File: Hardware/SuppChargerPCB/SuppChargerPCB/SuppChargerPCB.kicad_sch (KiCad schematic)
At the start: 36 parts, among them J1 SLIMSTACK, J2 SLIMSTACK, Q1 NMOS, Q2 NMOS, Q3 NMOS, Q4 NMOS, U1 BQ25756ERRVR

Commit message: reorg
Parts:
- removed RT1: 103AT-2, 103AT2, symbol NTC10k:103AT-2
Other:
- moved on the sheet: C1, C11, C5, C6, C7, D4, D5, J1, J2, L1, Q1, Q2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

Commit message: need to add connector symbols, desmos
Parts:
- removed C10, C3: 0.1uF, symbol Device:C
- removed C11: 100nF, symbol Device:C
- removed C4: 1uF, symbol Device:C
- removed C6, C7: 80uF, symbol Device:C
- removed C8: 0.47uF, symbol Device:C
- removed D4, D5: D, symbol Device:D
- removed L1: 10uH, symbol Device:L
- removed Q1, Q2, Q3, Q4: NMOS, symbol Simulation_SPICE:NMOS
- added C11, C20, C21, C22, C6, C7: 56uF, symbol Device:C_Polarized_US
- added C16, C17, C18, C19, C23, C25: 100nF, symbol Device:C
- added C24: 470nF, symbol Device:C
- added D10, D9: Schottky, symbol Device:D_Schottky
- added D6, D7: LED, symbol Device:LED
- added H1, H2, H3: MountingHole, symbol Mechanical:MountingHole
- added L3: 2.2uH, symbol Device:L
- added Q10, Q7, Q8, Q9: NMOS, symbol NMOS_Buck:SI3456DDV-T1-GE3
- added R12, R13: 0, symbol Device:R
- added R14: 2m, symbol Device:R
- added R15, R16, R18, R19: 10, symbol Device:R
- added R17: 5m, symbol Device:R
- added R20: 249k, symbol Device:R
- added R21: 14.11K, symbol Device:R
- added R22: 133k, symbol Device:R
- C1: value 100nF -> 470nF
- C2: value 0.47uF -> 1uF
- C5: value 100uF -> 4.7uF
- C9: value 0.1uF -> 100nF
- R1: value 5.24k -> 1000k
- R10: value 30.31k -> 10k
- R11: value R -> 10k
- R2: value 10k -> 16k
- R3: value 10k -> 42k
- R4: value 249k -> 0
- R5: value 0.05 -> 0
- R6: value 133k -> 0
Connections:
- net BAT is gone; now on net OUT: J2.1, J2.2, J2.3, J2.4, J2.5, J2.6, J2.7, J2.8
- net VAC is gone; now on an unnamed net: R2.1
- net *CE: now also J2.19, D6.1 (K)
- net *INT: now also J2.13, D7.1 (K)
- net +24V: now also C2.1, R1.1, U1.32 (VAC), U1.33 (VAC), C6.1, C7.1, R14.1, R15.1; no longer J1.24
- net BTST1: now also C16.2, D9.1 (K)
- net BTST2: now also C17.2, D10.1 (K)
- net DRV_SUP: now also R4.1
- net FB: now also R20.2, R21.1; no longer R11.1, R4.2
- net FBG: now also R21.2; no longer R11.2
- net HIDRV1: now also R5.1
- net LODRV1: now also R6.1, R12.2
- net LODRV2: now also R13.2
- net PGND: now also U1.8 (TS), C11.2, C18.2, C19.2, C20.2, C21.2, C22.2, C23.2, C25.2, C6.2, C7.2, Q10.1 (S), Q10.2 (S), Q10.3 (S), Q8.1 (S), Q8.2 (S), Q8.3 (S), R22.1; no longer J2.17, J2.19, R10.2, R6.2
- net REGN: no longer R1.1, R7.1, R8.1, R9.1
- net SCL: now also J2.11
- net SDA: now also J2.9
- net STAT1: now also J2.15
- net STAT2: now also J2.17
- net SW1: now also C16.1, L3.1, Q7.1 (S), Q7.2 (S), Q7.3 (S), Q8.5 (D), Q8.6 (S), Q8.7 (S), Q8.8 (S); no longer C1.1
- net SW2: now also C17.1, L3.2, Q10.5 (D), Q10.6 (S), Q10.7 (S), Q10.8 (S), Q9.1 (S), Q9.2 (S), Q9.3 (S)
- net at C9.1: now also C2.2; no longer U1.13 (SRN)
- net at R5.2: now also Q7.4 (G)
- net ACP: now reaches C1.2
- net ACP: now also U1.30 (ACP), C18.1, R15.2
- net FSW: now reaches U1.36 (FSW_SYNC)
- net FSW: now also R22.2; no longer R6.1
- net ACN: now reaches U1.29 (ACN)
- net ACN: now also C1.1, C19.1, R16.2
- net SRP: now reaches U1.14 (SRP)
- net SRP: now also C23.1, C24.2, R18.2
- net OUT: now reaches J2.10
- net OUT: now also J2.12, J2.14, J2.16, C21.1, C22.1, R17.2, R19.1, R20.1
- net at U1.34 (ACUV): now also R1.2; no longer R2.2
- net at R3.1, U1.35 (ACOV): now also R2.2
- removed net +BATT: R4.1, R5.1
- new net: C11.1, Q7.5 (D), Q7.6 (S), Q7.7 (S), Q7.8 (S), R14.2, R16.1
- new net: C20.1, Q9.5 (D), Q9.6 (S), Q9.7 (S), Q9.8 (S), R17.1, R18.1
- new net: Q10.4 (G), R13.1
- new net: D6.2 (A), R10.2
- new net: D10.2 (A), D9.2 (A), R4.2
- new net: Q9.4 (G), R12.1
- new net: Q8.4 (G), R6.2
- new net: D7.2 (A), R11.2
- new net +3V3: J1.24, R10.1, R11.1, R7.1, R8.1, R9.1
- new net SRN: C24.1, C25.1, R19.2, U1.13 (SRN)
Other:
- added sheet Misc (Misc.kicad_sch)
- note added: "*DRV_SUP on REGN power rail (~6V)"
- note added: "250kHz"
- note added: "4.2V is max charge cutoff 4.1 * 7 = 28.7V regulation target"
- note added: "Buck Boost @ 250 kHz"
- note added: "Feedback Voltage"
- note added: "Gate Drive Supply"
- note added: "Input Current Sense"
- note added: "Mounting Holes"
- note added: "NO REVERSE MODE! Clear the EN_REV register in software."
- note added: "NO TEMP SENSE! Clear the EN_TS register in software."
- note added: "Output Current Sense"
- note added: "Silkscreen"
- note added: "Switching Frequency Selection"
- note added: "UV - 20V OV - 30V"
- note added: "blue"
- note added: "green"
- note added: "red"
- note added: "shunt"
- note added: "tbd"
- note removed: "Boost Output"
- note removed: "Buck Input"
- note removed: "Buck-Boost"
- note removed: "Input Caps"
- note removed: "Output Cap"
- note removed: "Should be pulled up on LV Base (10k to logic voltage)"
- title: (none) -> Supp Charger
- moved on the sheet: D1, D2, D3, J1, J2, R7, R8, R9

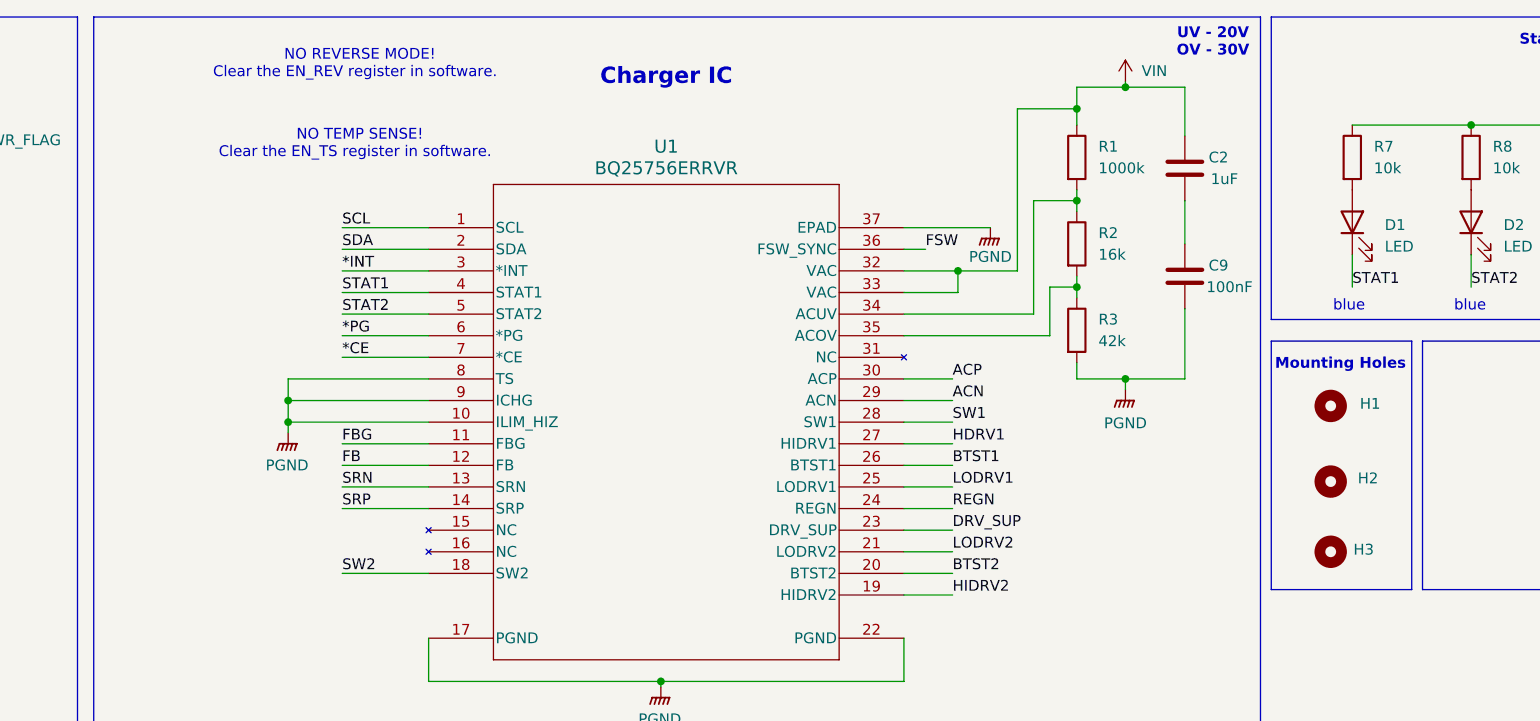
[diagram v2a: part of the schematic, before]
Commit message: added calcs, logic analyzer
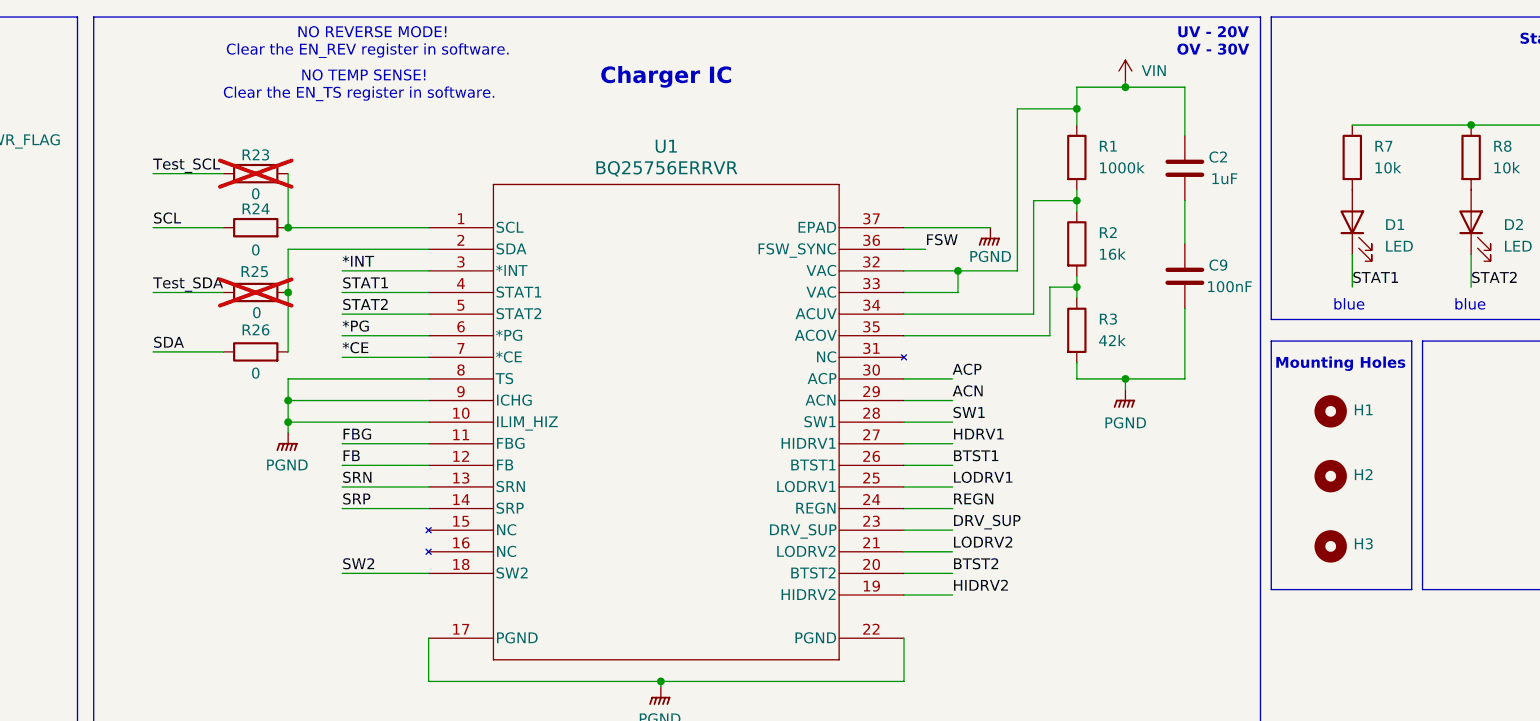
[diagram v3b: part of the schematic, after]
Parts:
- added R23, R24, R25, R26: 0, symbol Device:R
- H1, H2, H3: footprint (none) -> MountingHole:MountingHole_2.1mm
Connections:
- net SCL: now also R24.1; no longer U1.1 (SCL)
- net SDA: now also R26.1; no longer U1.2 (SDA)
- new net: R25.2, R26.2, U1.2 (SDA)
- new net: R23.2, R24.2, U1.1 (SCL)
- new net Test_SCL: R23.1
- new net Test_SDA: R25.1
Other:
- moved on the sheet: H1, H2, H3

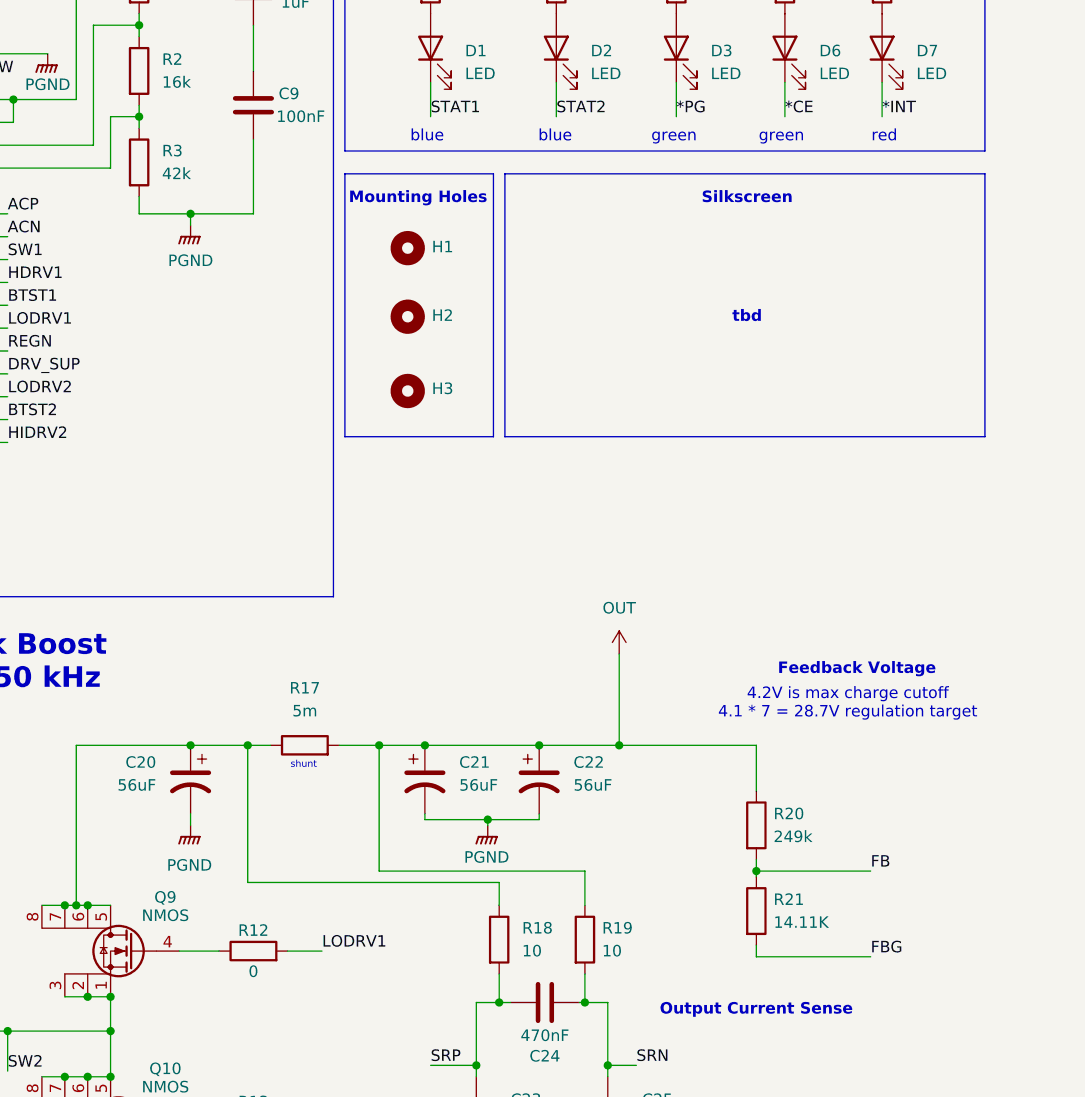
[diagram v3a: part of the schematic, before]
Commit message: need to assign bulk cap
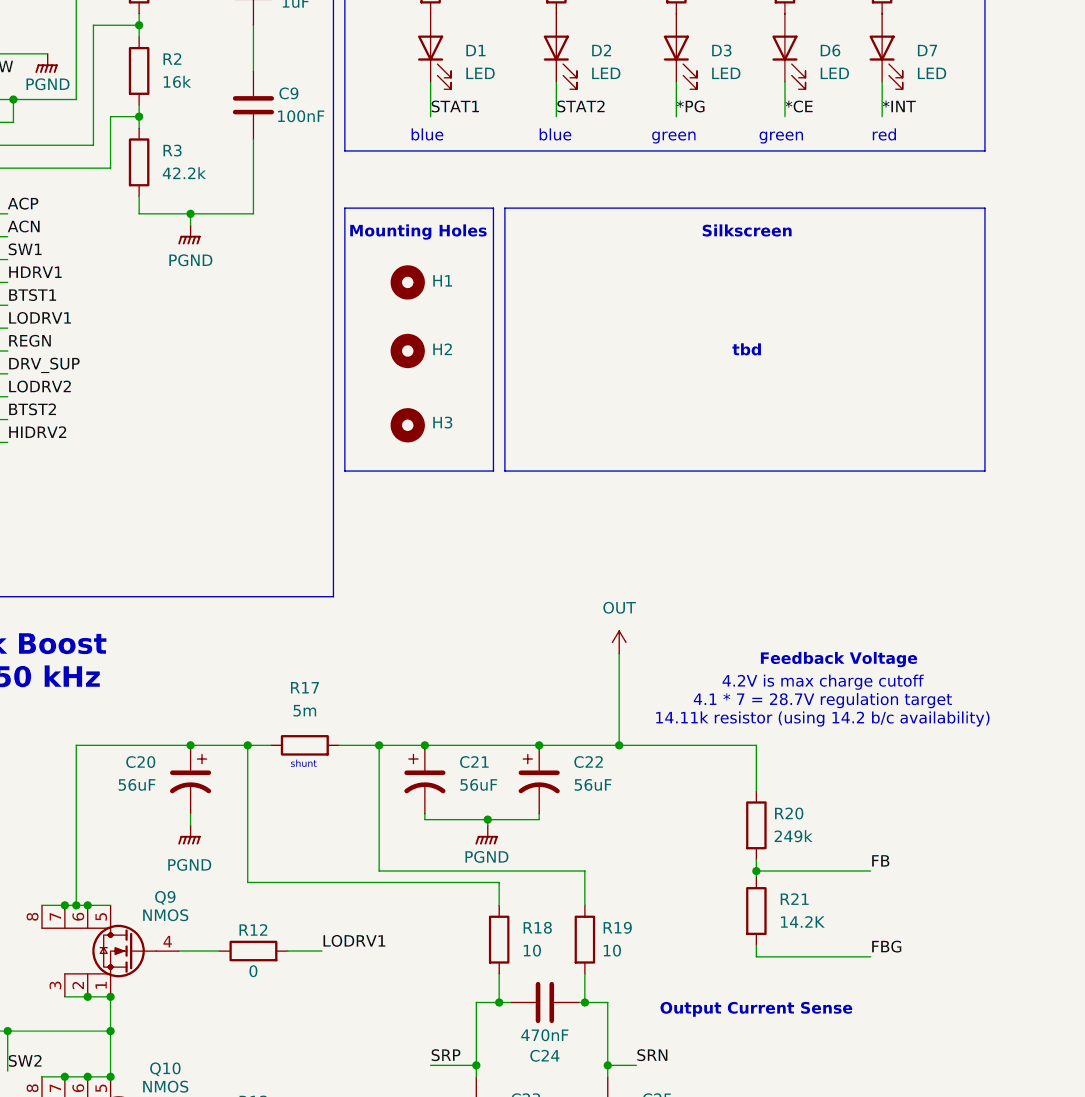
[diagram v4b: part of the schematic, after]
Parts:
- removed U1: BQ25756ERRVR, symbol BQIC:BQ25756ERRVR
- added U1: BQ25756ERRVR, Components:VQFN36_RRV_TEX, symbol Components:BQ25756ERRVR
- C1, C24: footprint (none) -> Capacitor_SMD:C_0603_1608Metric; P/N (none) -> UMK107ABJ474MA-T
- C11, C20, C21, C22, C6, C7: P/N (none) -> A770KS566M1JLAS031
- C16, C17, C18, C19, C23, C25, C9: footprint (none) -> Capacitor_SMD:C_0603_1608Metric; P/N (none) -> MLASH168SB7104KTNA01
- C2: footprint (none) -> Capacitor_SMD:C_0603_1608Metric; P/N (none) -> MLASU168SB5105KTNA01
- C5: footprint (none) -> Capacitor_SMD:C_0805_2012Metric; P/N (none) -> 08055D475KAT4A
- D1, D2: footprint (none) -> Diode_SMD:D_0603_1608Metric; P/N (none) -> LTST-C193TBKT-5A
- D10, D9: footprint (none) -> Components:SOD3716X145N
- D3, D6: footprint (none) -> Diode_SMD:D_0603_1608Metric; P/N (none) -> 150060GS75000
- D7: footprint (none) -> Diode_SMD:D_0603_1608Metric; P/N (none) -> LS Q976.01-N1Q2-1
- H1, H2, H3: footprint MountingHole:MountingHole_2.1mm -> MountingHole:MountingHole_3.2mm_M3
- L3: footprint (none) -> Components:HCM1A0503V22R2R; P/N (none) -> HCM1A0503V2-2R2-R
- R1: footprint (none) -> Resistor_SMD:R_0603_1608Metric; P/N (none) -> RCA06031M00FKEASR
- R10, R11, R7, R8, R9: footprint (none) -> Resistor_SMD:R_0603_1608Metric; P/N (none) -> CRCW060310K0FKEI
- R12, R13, R4, R5, R6: footprint (none) -> Resistor_SMD:R_0603_1608Metric
- R14: footprint (none) -> Resistor_SMD:R_0603_1608Metric; P/N (none) -> RV0603FR-072ML
- R15, R16, R18, R19: footprint (none) -> Resistor_SMD:R_0603_1608Metric; P/N (none) -> CRCW060310R0FKEE
- R17: footprint (none) -> Resistor_SMD:R_0603_1608Metric; P/N (none) -> CFN0603-JZ-R005ELF
- R2: footprint (none) -> Resistor_SMD:R_0603_1608Metric; P/N (none) -> CRCW060316K0FKTA
- R20: footprint (none) -> Resistor_SMD:R_0603_1608Metric; P/N (none) -> MCT06030D2493BP500
- R21: value 14.11K -> 14.2K; footprint (none) -> Resistor_SMD:R_0603_1608Metric; P/N (none) -> TNPW060314K2BEEN
- R22: footprint (none) -> Resistor_SMD:R_0603_1608Metric; P/N (none) -> RC0603FR-07133KL
- R23, R24, R25, R26: footprint (none) -> Resistor_SMD:R_0603_1608Metric; P/N (none) -> CRCW06030000Z0EE
- R3: value 42k -> 42.2k; footprint (none) -> Resistor_SMD:R_0603_1608Metric; P/N (none) -> CR0603-FX-4222ELF
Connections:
- net *CE: now also U1.7 (*CE)
- net *INT: now also U1.3 (*INT)
- net *PG: now also U1.6 (*PG)
- net +24V: now also U1.32 (VAC), U1.33 (VAC)
- net ACN: now also U1.29 (ACN)
- net ACP: now also U1.30 (ACP)
- net BTST1: now also U1.26 (BTST1)
- net BTST2: now also U1.20 (BTST2)
- net DRV_SUP: now also U1.23 (DRV_SUP)
- net FB: now also U1.12 (FB)
- net FBG: now also U1.11 (FBG)
- net FSW: now also U1.36 (FSW_SYNC)
- net HDRV1: now also U1.27 (HIDRV1)
- net HIDRV2: now also U1.19 (HIDRV2)
- net LODRV1: now also U1.25 (LODRV1)
- net LODRV2: now also U1.21 (LODRV2)
- net PGND: now also U1.10 (ILIM_HIZ), U1.17 (PGND), U1.22 (PGND), U1.37 (EPAD), U1.8 (TS), U1.9 (ICHG)
- net REGN: now also U1.24 (REGN)
- net SRN: now also U1.13 (SRN)
- net SRP: now also U1.14 (SRP)
- net STAT1: now also U1.4 (STAT1)
- net STAT2: now also U1.5 (STAT2)
- net SW1: now also U1.28 (SW1)
- net SW2: now also U1.18 (SW2)
- net at R25.2, R26.2: now also U1.2 (SDA)
- net at R23.2, R24.2: now also U1.1 (SCL)
- net at R1.2, R2.1: now also U1.34 (ACUV)
- net at R2.2, R3.1: now also U1.35 (ACOV)
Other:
- note added: "4.2V is max charge cutoff 4.1 * 7 = 28.7V regulation target 14.11k resistor (using 14.2 b/c availability)"
- note removed: "4.2V is max charge cutoff 4.1 * 7 = 28.7V regulation target"
- moved on the sheet: H1, H2, H3

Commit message: abused pwr flags
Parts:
- removed R22: 133k, Resistor_SMD:R_0603_1608Metric, symbol Device:R
- added C10, C8: 4.7uF, Capacitor_SMD:C_0805_2012Metric, symbol Device:C
- added R29: 133k, Resistor_SMD:R_0603_1608Metric, symbol Device:R
- added R30: 10, Resistor_SMD:R_0603_1608Metric, symbol Device:R
- added R31, R32: 0, Resistor_SMD:R_0603_1608Metric, symbol Device:R
- C11, C20, C21, C22, C6, C7: footprint (none) -> Components:CAPAE830X1050N; P/N A770KS566M1JLAS031 -> 865080653014
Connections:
- net HDRV1 is gone; now on net HIDRV1: U1.27 (HIDRV1)
- net DRV_SUP: now also C10.1, R30.2
- net HIDRV2: now also R12.2
- net LODRV1: no longer R12.2
- net PGND: now also C10.2, C8.2, R29.1; no longer J1.1, J1.10, J1.2, J1.3, J1.4, J1.5, J1.6, J1.7, J1.8, J1.9, U1.22 (PGND)
- net FSW: no longer names the net of U1.36 (FSW_SYNC)
- net FSW: now also R29.2
- net REGN: no longer names the net of U1.24 (REGN)
- net REGN: now also C8.1, R30.1
- new net: R31.1, R32.1, U1.22 (PGND)
- new net GND: J1.1, J1.10, J1.2, J1.3, J1.4, J1.5, J1.6, J1.7, J1.8, J1.9, R32.2
- new net GND_TEST: R31.2
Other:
- note removed: "Switching Frequency Selection"

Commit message: pre sheet reorg
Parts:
- removed C22, C7: 56uF, Components:CAPAE830X1050N, symbol Device:C_Polarized_US
- removed R31, R32: 0, Resistor_SMD:R_0603_1608Metric, symbol Device:R
- C11, C20, C21, C6: value 56uF -> 82uF; P/N 865080653014 -> A759MS826M1JAAE050
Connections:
- net GND is gone; now on net PGND: J1.1, J1.10, J1.2, J1.3, J1.4, J1.5, J1.6, J1.7, J1.8, J1.9
- net PGND: now also U1.22 (PGND)
- net at C9.1: no longer C2.2
- net ACUV: now reaches R1.2, R2.1, U1.34 (ACUV)
- net ACOV: now reaches R2.2, R3.1, U1.35 (ACOV)
- net Test_SDA: no longer names the net of R25.1
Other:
- sheet Misc ports: added SDA; removed none
- note added: "MAKE OWN SHEET"
- note added: "add 24v, out LEDs"
- note added: "add pullup 3v3"
- note added: "separate pullups for status signals"
- moved on the sheet: C2, C21, C6
